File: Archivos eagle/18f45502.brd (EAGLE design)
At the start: 87.6 x 53 mm, 27 parts, among them IC1 PIC18F4550_40, IC2 7805DT, Q1 20MHz, X2 PN61729-S

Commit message: build alpha 1.4.1
arregle el tema de la masa que quedaba separada, puse un puente que
queda oculto debajo del micro
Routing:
- net GND: track 27.6 -> 37.7 mm, vias 0 -> 2
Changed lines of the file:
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@@
 <contactref element="C6" pad="2"/>
 <contactref element="X2" pad="4"/>
-<wire x1="46.99" y1="5.08" x2="50.8" y2="2.54" width="0" layer="19" extent="16-16"/>
+<via x="46.99" y="22.86" extent="1-16" drill="0.6"/>
+<via x="52.07" y="22.86" extent="1-16" drill="0.6"/>
+<wire x1="52.07" y1="22.86" x2="52.07" y2="21.59" width="0.3048" layer="16"/>
+<wire x1="46.99" y1="22.86" x2="46.99" y2="19.05" width="0.3048" layer="16"/>
+<wire x1="46.99" y1="22.86" x2="52.07" y2="22.86" width="0.3048" layer="1"/>
 </signal>
 <signal name="N$3">

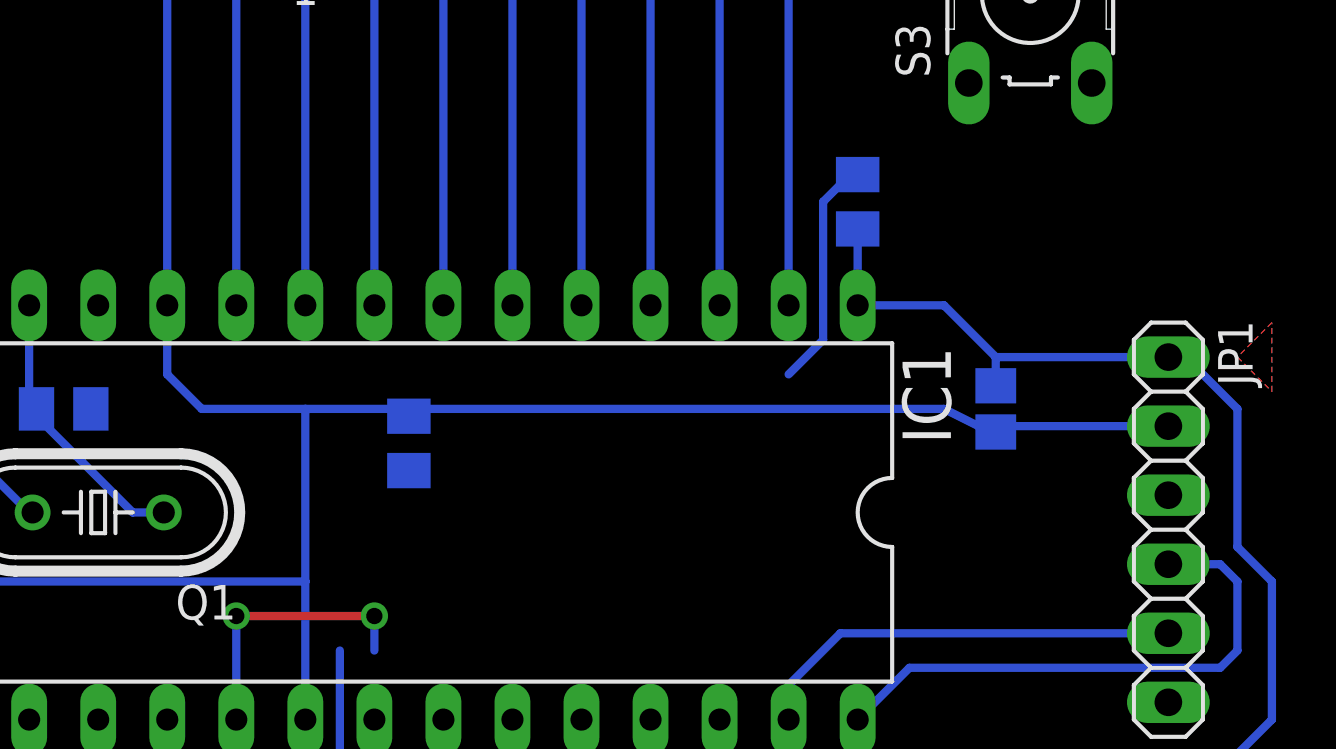
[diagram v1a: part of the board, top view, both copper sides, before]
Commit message: build alpha 1.5.1
se agrego una resistencia de pull up en el pulsador de bootloader (super
importante)
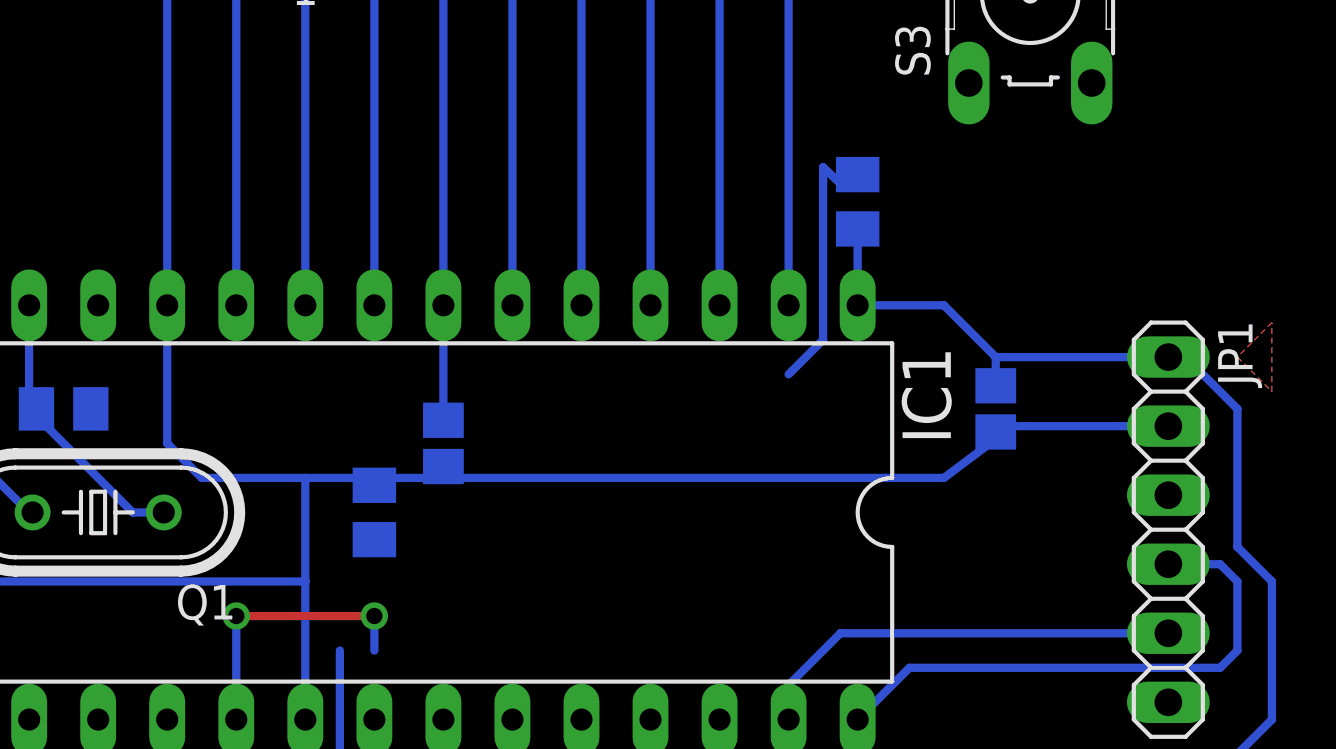
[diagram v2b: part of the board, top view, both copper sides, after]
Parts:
- added R5: 10k, resistor:R0805
- moved C6 2.84 mm to (52.1, 26.7)
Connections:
- net N$18: now also R5.2
- net VDD: now also R5.1
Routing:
- net N$18: track 36.0 -> 40.2 mm
- net GND: track 37.7 -> 39.0 mm
- net VDD: track 169.5 -> 170.4 mm
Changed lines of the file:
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@@
 <attribute name="VALUE" x="1.27" y="5.08" size="1.27" layer="27"/>
 </element>
-<element name="C6" library="resistor" package="C0805K" value="100n" x="53.34" y="29.21" smashed="yes" rot="MR270">
-<attribute name="NAME" x="52.324" y="30.2006" size="1.016" layer="26" rot="MR270"/>
-<attribute name="VALUE" x="55.24" y="30.21" size="1.016" layer="28" rot="MR270"/>
+<element name="C6" library="resistor" package="C0805K" value="100n" x="52.07" y="26.67" smashed="yes" rot="MR270">
+<attribute name="NAME" x="51.054" y="27.6606" size="1.016" layer="26" rot="MR270"/>
+<attribute name="VALUE" x="53.97" y="27.67" size="1.016" layer="28" rot="MR270"/>
 </element>
 <element name="C7" library="rcl" package="TT2D5L" value="47u" x="24.13" y="27.94" rot="R270"/>
@@
 <element name="C1" library="resistor" package="C0805K" value=".1uF" x="15.24" y="27.94" rot="MR90"/>
 <element name="C2" library="resistor" package="C0805K" value=".33uF" x="15.24" y="31.75" rot="MR90"/>
+<element name="R5" library="resistor" package="R0805" value="10k" x="54.61" y="29.21" rot="MR90"/>
 </elements>
 <signals>
@@
 <wire x1="49.53" y1="3.81" x2="49.53" y2="5.08" width="0.3048" layer="16"/>
 <wire x1="49.53" y1="19.05" x2="49.53" y2="24.13" width="0.3048" layer="16"/>
-<wire x1="49.53" y1="24.13" x2="49.53" y2="30.48" width="0.3048" layer="16"/>
-<wire x1="49.53" y1="30.48" x2="53.34" y2="30.48" width="0.3048" layer="16"/>
-<wire x1="53.34" y1="30.48" x2="73.025" y2="30.48" width="0.3048" layer="16"/>
-<wire x1="73.025" y1="30.48" x2="74.295" y2="29.845" width="0.3048" layer="16"/>
-<wire x1="74.295" y1="29.845" x2="81.28" y2="29.845" width="0.3048" layer="16"/>
-<wire x1="74.295" y1="29.845" x2="74.93" y2="29.63" width="0.3048" layer="16"/>
+<wire x1="49.53" y1="24.13" x2="49.53" y2="27.94" width="0.3048" layer="16"/>
+<wire x1="49.53" y1="27.94" x2="52.07" y2="27.94" width="0.3048" layer="16"/>
+<wire x1="52.07" y1="27.94" x2="54.61" y2="27.94" width="0.3048" layer="16"/>
+<wire x1="54.61" y1="27.94" x2="73.025" y2="27.94" width="0.3048" layer="16"/>
+<wire x1="73.025" y1="27.94" x2="75.565" y2="29.845" width="0.3048" layer="16"/>
+<wire x1="75.565" y1="29.845" x2="81.28" y2="29.845" width="0.3048" layer="16"/>
+<wire x1="75.565" y1="29.845" x2="74.93" y2="29.63" width="0.3048" layer="16"/>
 <contactref element="IC2" pad="2"/>
 <contactref element="C1" pad="1"/>
@@
 <wire x1="17.78" y1="22.86" x2="19.05" y2="24.13" width="0.3048" layer="16"/>
 <wire x1="19.05" y1="24.13" x2="49.53" y2="24.13" width="0.3048" layer="16"/>
-<wire x1="53.34" y1="30.21" x2="53.34" y2="30.48" width="0.3048" layer="16"/>
-<wire x1="44.45" y1="34.29" x2="44.45" y2="31.75" width="0.3048" layer="16"/>
-<wire x1="44.45" y1="31.75" x2="45.72" y2="30.48" width="0.3048" layer="16"/>
-<wire x1="45.72" y1="30.48" x2="49.53" y2="30.48" width="0.3048" layer="16"/>
+<wire x1="52.07" y1="27.67" x2="52.07" y2="27.94" width="0.3048" layer="16"/>
+<wire x1="44.45" y1="34.29" x2="44.45" y2="29.21" width="0.3048" layer="16"/>
+<wire x1="44.45" y1="29.21" x2="45.72" y2="27.94" width="0.3048" layer="16"/>
+<wire x1="45.72" y1="27.94" x2="49.53" y2="27.94" width="0.3048" layer="16"/>
+<contactref element="R5" pad="1"/>
+<wire x1="54.61" y1="28.36" x2="54.61" y2="27.94" width="0.3048" layer="16"/>
 </signal>
 <signal name="RB6">
@@
 <contactref element="X2" pad="S2"/>
 <wire x1="69.23" y1="38.75" x2="69.85" y2="39.1" width="0.3048" layer="16"/>
-<wire x1="68.58" y1="38.1" x2="69.23" y2="38.75" width="0.3048" layer="16"/>
-<wire x1="68.58" y1="33.02" x2="68.58" y2="38.1" width="0.3048" layer="16"/>
+<wire x1="68.58" y1="39.37" x2="69.23" y2="38.75" width="0.3048" layer="16"/>
+<wire x1="68.58" y1="33.02" x2="68.58" y2="39.37" width="0.3048" layer="16"/>
 <wire x1="67.31" y1="31.75" x2="68.58" y2="33.02" width="0.3048" layer="16"/>
 <wire x1="50.8" y1="2.54" x2="50.8" y2="21.59" width="0.3048" layer="16"/>
@@
 <wire x1="72.39" y1="50.8" x2="73.66" y2="49.53" width="0.3048" layer="16"/>
 <wire x1="73.66" y1="49.53" x2="73.9394" y2="48.9712" width="0.3048" layer="16"/>
+<contactref element="R5" pad="2"/>
+<wire x1="54.61" y1="34.29" x2="54.61" y2="30.06" width="0.3048" layer="16"/>
 </signal>
 <signal name="N$19">
